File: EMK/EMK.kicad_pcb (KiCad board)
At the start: 4 copper layers, 112.2 x 87.7 mm, 122 parts, among them J1 USB_C_Receptacle_USB2.0_14P, J2 Conn_01x02_Socket, J3 Conn_ARM_JTAG_SWD_10, Q1 Si2371EDS, Q2 Si2371EDS, SW1 SW_Nidec_CAS-120A1, SW10 MX3, SW11 MX7, SW12 MX11, SW13 MX15, SW14 MX4, SW15 MX8, SW16 MX12, SW17 MX16, SW18 SW_Push, SW19 SW_Nidec_CAS-120A1, SW2 MX1, SW20 Mode Switch, SW3 MX5, SW4 MX9, SW5 MX13, SW6 MX2, SW7 MX6, SW8 MX10, SW9 MX14, U1 nRF52840-QFAA, U2 15nH, U3 TPS62822DLC, U4 USBLC6-2SC6, U5 TP4057, Y1 Crystal_32.768kHz, Y2 Crystal_32mHz

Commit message: Alimentação - Fix
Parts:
- moved J2 11.4 mm to (121.3, 43.8)
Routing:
- net VBAT: track 68.1 -> 25.3 mm
- net MCU_VDD_RGB: track 34.4 -> 25.0 mm
- net SWCLK: track 61.8 -> 64.4 mm
- net VDD_NRF: track 140.4 -> 139.0 mm
- net (no net): track 1.40 -> 0.00 mm
- net SWDIO: track 62.7 -> 63.8 mm
- net Net-(U3-FB): track 12.6 -> 12.1 mm
- added copper zone on In2.Cu, net RGB_VDD
- added copper zone on In2.Cu, net VBAT

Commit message: Finalização
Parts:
- moved R9 6.67 mm to (142.3, 49.8), turned to 0 degrees
- moved C9 1.75 mm to (148.0, 70.7)
- moved C11 0.22 mm to (146.8, 57.5)
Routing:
- net RGB_VDD: track 456.8 -> 78.9 mm
- net VBUS: track 91.1 -> 71.0 mm, vias 5 -> 7
- net VDD_NRF: track 139.0 -> 130.6 mm, vias 9 -> 8
- net VBAT: track 25.3 -> 32.8 mm, vias 4 -> 3
- net MATRIX_M1: track 82.8 -> 75.3 mm, vias 1 -> 2
- net NRST: track 78.8 -> 72.2 mm, vias 2 -> 3
- net Net-(D3-K): track 31.0 -> 37.1 mm
- net MATRIX_M2: track 74.3 -> 79.2 mm, vias 1 -> 2
- net COL3: track 204.1 -> 208.9 mm
- net Net-(D7-A): track 11.4 -> 16.0 mm, vias 0 -> 1
- net Net-(U1-P0.04/AIN2): track 7.24 -> 11.8 mm
- net MATRIX_M3: track 73.4 -> 77.1 mm, vias 1 -> 2
- net GND: track 110.1 -> 106.6 mm, vias 60 -> 59
- net SWDIO: track 63.8 -> 66.8 mm
- net SWCLK: track 64.4 -> 66.1 mm
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- added copper zone on In2.Cu, net GND
- added copper zone on F.Cu, net RGB_VDD
- added copper zone on F.Cu, net VBAT
- added copper zone on B.Cu, net VBUS
- added copper zone on B.Cu, net VDD_NRF
- removed copper zone on In2.Cu, net RGB_VDD
- removed copper zone on In2.Cu, net VBAT
- removed copper zone on In2.Cu, net VDD_NRF
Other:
- board size 112.2 x 87.7 mm -> 114.1 x 92.5 mm

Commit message: Finalização
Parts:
- removed U4: USBLC6-2SC6, Package_TO_SOT_SMD:SOT-23-6
- moved R2 11.4 mm to (121.9, 32.5), turned to 90 degrees
- moved R1 8.51 mm to (123.5, 32.5), turned to 90 degrees
- moved Q1 0.45 mm to (137.8, 35.3)
- moved R3 0.45 mm to (140.2, 37.1)
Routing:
- net Net-(J1-CC2): track 3.44 -> 14.1 mm
- net VBUS: track 71.0 -> 63.2 mm, vias 7 -> 6
- net Net-(J1-CC1): track 4.49 -> 10.1 mm, vias 0 -> 2
- net Net-(D3-K): track 37.1 -> 32.0 mm
- net Net-(D2-K): track 26.6 -> 23.5 mm, vias 3 -> 4
- net GND: track 106.6 -> 109.4 mm, vias 59 -> 58
- net ON_LED: track 37.8 -> 38.8 mm
- net NRST: track 72.2 -> 73.1 mm
- net Net-(Q1-D): track 8.58 -> 7.92 mm
- net RGB_VDD: track 78.9 -> 79.6 mm, vias 17 -> 18
- net VBAT: track 32.8 -> 33.4 mm
- net Net-(D1-K): track 11.0 -> 11.6 mm
- added copper zone on F.Cu, net VBUS

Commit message: Remap tracement
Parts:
- removed C19: 1.5pF, Capacitor_SMD:C_0603_1608Metric
- removed R10: 0, Resistor_SMD:R_0603_1608Metric
- added L4: 2.7nH, Inductor_SMD:L_0603_1608Metric, B.Cu at (143.8, 122.5)
- AE1: footprint RF_Antenna:Johanson_2450AT43F0100 -> RF_Antenna:Johanson_2450AT18x100
- moved SW20 64.1 mm to (149.8, 67.2), turned to 90 degrees
- moved J3 44.7 mm to (141.3, 60.4), turned to 0 degrees
- moved C12 28.6 mm to (139.7, 94.7)
- moved C11 27.5 mm to (148.4, 85.0)
- moved C13 27.5 mm to (135.5, 84.4)
- moved Y1 27.5 mm to (143.1, 83.5)
- moved C1 27.5 mm to (142.3, 80.8)
- moved C2 27.5 mm to (143.9, 80.8)
- moved C3 27.5 mm to (141.6, 101.3)
- moved C4 27.5 mm to (140.1, 101.3)
- moved C5 27.5 mm to (140.6, 80.8)
- moved C6 27.5 mm to (143.5, 101.2)
- moved C7 27.5 mm to (140.4, 89.8)
- moved C8 27.5 mm to (141.1, 86.3)
- moved C9 27.5 mm to (149.6, 98.2)
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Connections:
- C20 pad 2: GND -> ANT_BT
- J1 pad A6: J_D+ -> unconnected-(J1-D+-PadA6)
- J1 pad A7: J_D- -> unconnected-(J1-D--PadA7)
- J1 pad B6: J_D+ -> unconnected-(J1-D+-PadB6)
- J1 pad B7: J_D- -> unconnected-(J1-D--PadB7)
- L3 pad 1: Net-(C20-Pad1) -> Net-(AE1-A)
- L3 pad 2: ANT_BT -> Net-(C20-Pad1)
- U1 pad 18: ROW1 -> unconnected-(U1-P0.19-Pad18)
- U1 pad 19: ROW0 -> unconnected-(U1-P0.20-Pad19)
- U1 pad 21: ROW3 -> unconnected-(U1-P0.22-Pad21)
- U1 pad 23: RGB_SIG -> unconnected-(U1-P0.24-Pad23)
- U1 pad 39: unconnected-(U1-P0.03/AIN1-Pad39) -> COL1
- U1 pad 40: unconnected-(U1-P0.02/AIN0-Pad40) -> COL2
- U1 pad 41: unconnected-(U1-P0.28/AIN4-Pad41) -> COL3
- U1 pad 42: COL1 -> ROW0
- U1 pad 43: COL3 -> ROW1
- U1 pad 44: COL2 -> ROW2
- U1 pad 6: unconnected-(U1-P0.07/TRACECLK-Pad6) -> ROW3
- U1 pad 8: unconnected-(U1-P1.08-Pad8) -> RGB_SIG
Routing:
- net VDD_NRF: track 130.6 -> 51.4 mm
- net MATRIX_M2: track 79.2 -> 4.25 mm, vias 2 -> 1
- net MATRIX_M3: track 77.1 -> 2.19 mm, vias 2 -> 1
- net MATRIX_M1: track 75.3 -> 4.74 mm, vias 2 -> 1
- net SWCLK: track 66.1 -> 1.81 mm
- net SWDIO: track 66.8 -> 2.58 mm, vias 2 -> 1
- net ROW0: track 135.2 -> 74.6 mm, vias 2 -> 1
- net COL0: track 140.9 -> 93.3 mm
- net NRST: track 73.1 -> 34.7 mm, vias 3 -> 2
- net ROW1: track 109.1 -> 74.8 mm, vias 2 -> 0
- net ROW3: track 105.3 -> 74.2 mm, vias 2 -> 1
- net ROW2: track 104.4 -> 73.6 mm, vias 2 -> 1
- net COL2: track 189.2 -> 160.0 mm, vias 3 -> 1
- net ANT_BT: track 29.5 -> 1.01 mm
- net COL3: track 208.9 -> 183.6 mm, vias 3 -> 1
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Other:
- board size 114.1 x 92.5 mm -> 114.1 x 105.2 mm

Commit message: Remap tracement
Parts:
- C20: footprint Capacitor_SMD:C_0603_1608Metric -> Capacitor_SMD:C_0402_1005Metric
- L3: footprint Inductor_SMD:L_0603_1608Metric -> Inductor_SMD:L_0402_1005Metric
- L4: footprint Inductor_SMD:L_0603_1608Metric -> Inductor_SMD:L_0402_1005Metric_Pad0.77x0.64mm_HandSolder
- moved R13 55.5 mm to (143.4, 51.8), turned to -90 degrees
- moved Q2 25.3 mm to (147.2, 51.9)
- moved R7 21.9 mm to (131.5, 47.5)
- moved C18 21.6 mm to (128.4, 47.4), turned to -90 degrees
- moved R9 21.5 mm to (144.1, 71.2), turned to -90 degrees
- moved U5 18.1 mm to (129.4, 43.6)
- moved J3 10.9 mm to (137.1, 70.4)
- moved C21 9.37 mm to (145.1, 99.3)
- moved R11 7.85 mm to (145.3, 64.8), turned to 0 degrees
- moved L4 4.36 mm to (147.1, 119.7), turned to 0 degrees
- moved C10 2.75 mm to (149.1, 96.4)
- moved C9 2.57 mm to (150.7, 95.9)
- moved C11 2.26 mm to (150.5, 84.2)
- moved C20 2.19 mm to (147.7, 118.2)
- moved L3 1.70 mm to (147.8, 121.2)
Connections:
- SW20 pad 1: MATRIX_M1 -> MATRIX_M3
- SW20 pad 4: MATRIX_M3 -> MATRIX_M1
- U1 pad 10: unconnected-(U1-P0.11/TRACEDATA2-Pad10) -> MATRIX_M2
- U1 pad 11: unconnected-(U1-P0.12/TRACEDATA1-Pad11) -> MATRIX_M3
- U1 pad 13: MATRIX_M3 -> unconnected-(U1-P0.13-Pad13)
- U1 pad 14: MATRIX_M2 -> unconnected-(U1-P0.14-Pad14)
- U1 pad 15: MATRIX_M1 -> unconnected-(U1-P0.17-Pad15)
- U1 pad 20: ROW2 -> unconnected-(U1-P0.21-Pad20)
- U1 pad 7: RGB_ON -> RGB_SIG
- U1 pad 8: RGB_SIG -> RGB_ON
- U1 pad 9: unconnected-(U1-P1.09/TRACEDATA3-Pad9) -> MATRIX_M1
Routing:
- net ON_LED: track 19.5 -> 70.8 mm, vias 1 -> 3
- net ROW3: track 74.2 -> 123.1 mm, vias 1 -> 0
- net NRST: track 34.7 -> 78.8 mm, vias 2 -> 3
- net RGB_SIG: track 94.8 -> 133.6 mm, vias 1 -> 2
- net RGB_ON: track 0.00 -> 38.5 mm
- net VBUS: track 57.9 -> 23.7 mm, vias 6 -> 5
- net ROW2: track 73.6 -> 105.3 mm, vias 1 -> 0
- net SWCLK: track 1.81 -> 29.8 mm, vias 2 -> 1
- net SWDIO: track 2.58 -> 29.9 mm
- net MATRIX_M1: track 4.74 -> 31.5 mm, vias 1 -> 0
- net ROW0: track 74.6 -> 99.4 mm, vias 1 -> 0
- net MATRIX_M2: track 4.25 -> 27.3 mm, vias 1 -> 0
- net MATRIX_M3: track 2.19 -> 24.1 mm, vias 1 -> 0
- net Net-(D2-K): track 23.5 -> 44.3 mm
- net VBAT: track 29.0 -> 49.1 mm
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- added copper zone on B.Cu, net GND
- added copper zone on B.Cu, net VBAT
- added copper zone on F.Cu, net VDD_NRF

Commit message: Refatora a antena
Ajusta a antena.
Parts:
- C20: value 1pF -> 1.2pF
- L3: value 3.9nH -> 3.3nH
- moved C20 2.98 mm to (150.0, 120.1)
- moved L4 2.90 mm to (149.4, 121.5)
- moved L3 2.84 mm to (150.0, 123.0)
- moved AE1 2.44 mm to (150.0, 126.5)
- moved C21 2.38 mm to (145.7, 97.0), turned to 0 degrees
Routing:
- net ANT_BT: track 4.42 -> 27.6 mm
- net Net-(AE1-A): track 2.31 -> 1.56 mm
- net GND: vias 61 -> 105
- net (no net): vias 0 -> 13
- removed copper zone on In1.Cu, net GND

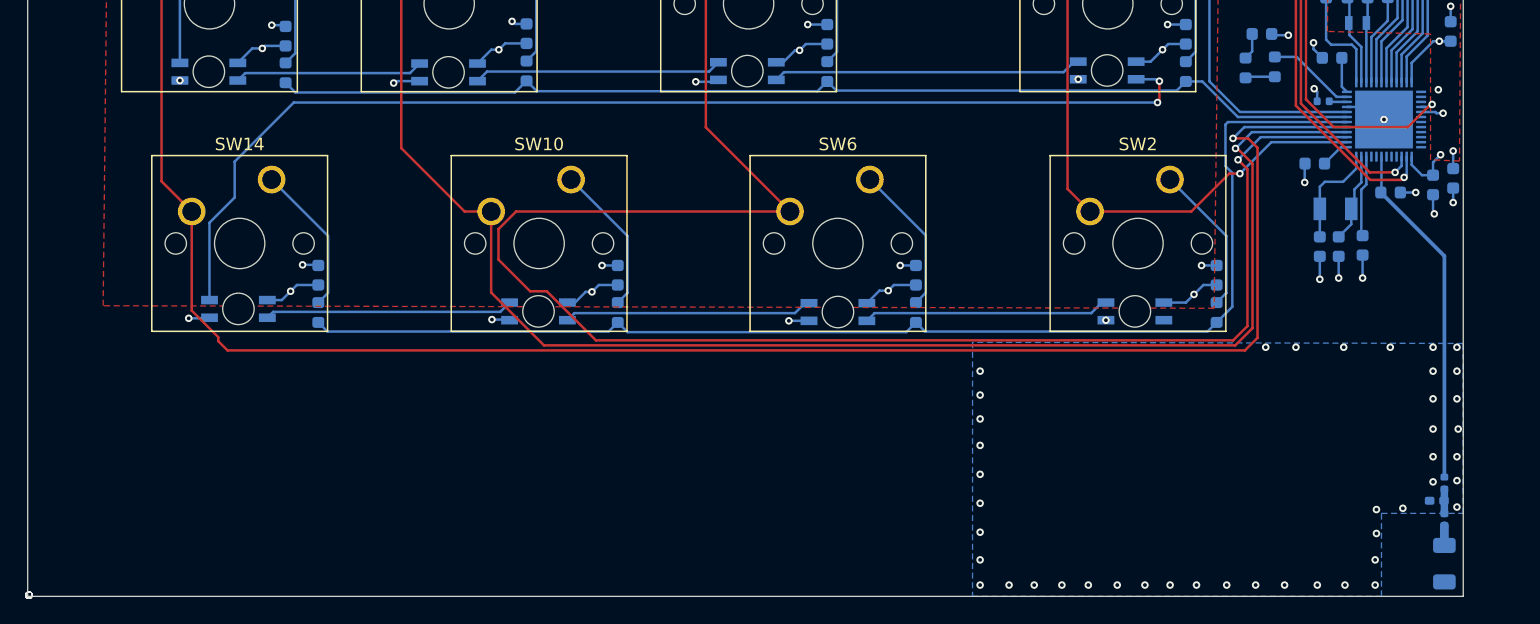
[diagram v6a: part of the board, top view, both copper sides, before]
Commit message: Corrige problemas de vias
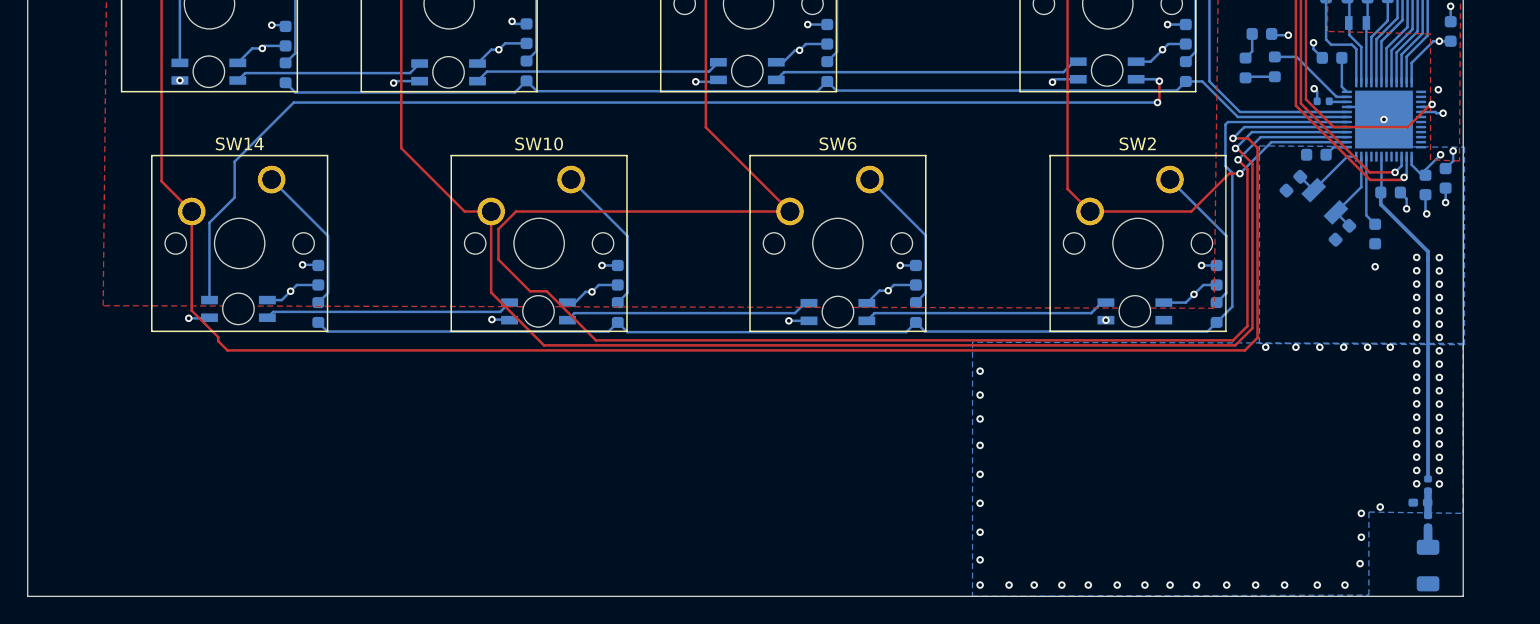
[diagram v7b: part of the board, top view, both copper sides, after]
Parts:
- moved C4 5.42 mm to (138.0, 96.3), turned to 45 degrees
- moved C6 1.35 mm to (144.5, 100.3)
- moved AE1 1.31 mm to (148.7, 126.7)
- moved C20 1.31 mm to (148.7, 120.2)
- moved L3 1.31 mm to (148.7, 123.2)
- moved L4 1.31 mm to (148.1, 121.7)
- moved C3 1.14 mm to (141.9, 100.2), turned to 45 degrees
- moved Y2 1.04 mm to (140.5, 97.7), turned to 135 degrees
- moved C12 0.71 mm to (139.8, 94.0)
- moved C10 0.60 mm to (148.5, 96.4)
- moved C9 0.60 mm to (150.1, 95.9)
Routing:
- net GND: track 83.0 -> 78.5 mm, vias 105 -> 126
- net Net-(U1-XC2): track 8.53 -> 6.00 mm
- net Net-(U1-DEC3): track 6.48 -> 5.66 mm
- net (no net): vias 13 -> 0
